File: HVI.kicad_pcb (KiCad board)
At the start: 2 copper layers, 48 x 48 mm, 47 parts, among them J1 Conn_01x02, J2 Conn_01x02, J3 Conn_01x02, U1 VIPER06-SSOP-10

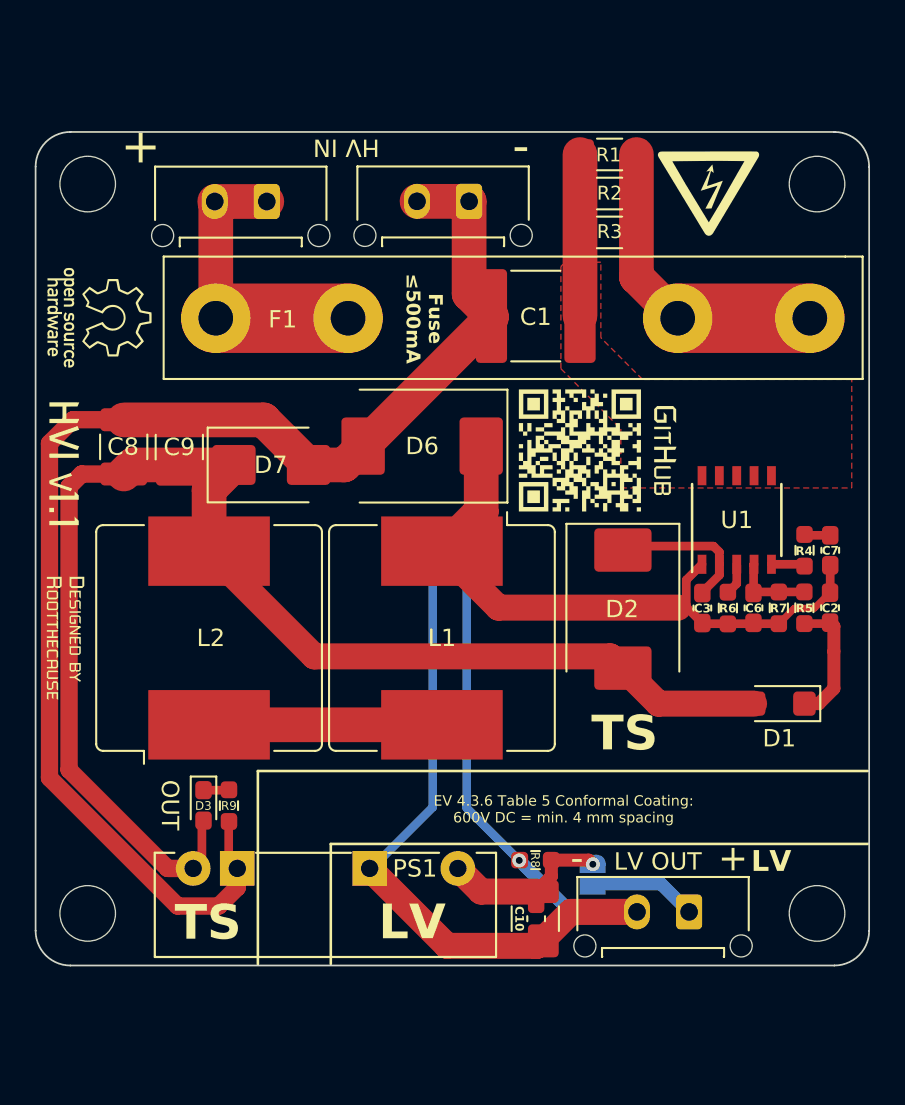
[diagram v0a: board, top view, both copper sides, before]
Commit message: Changed the connectors to Molex MicrofitPlus
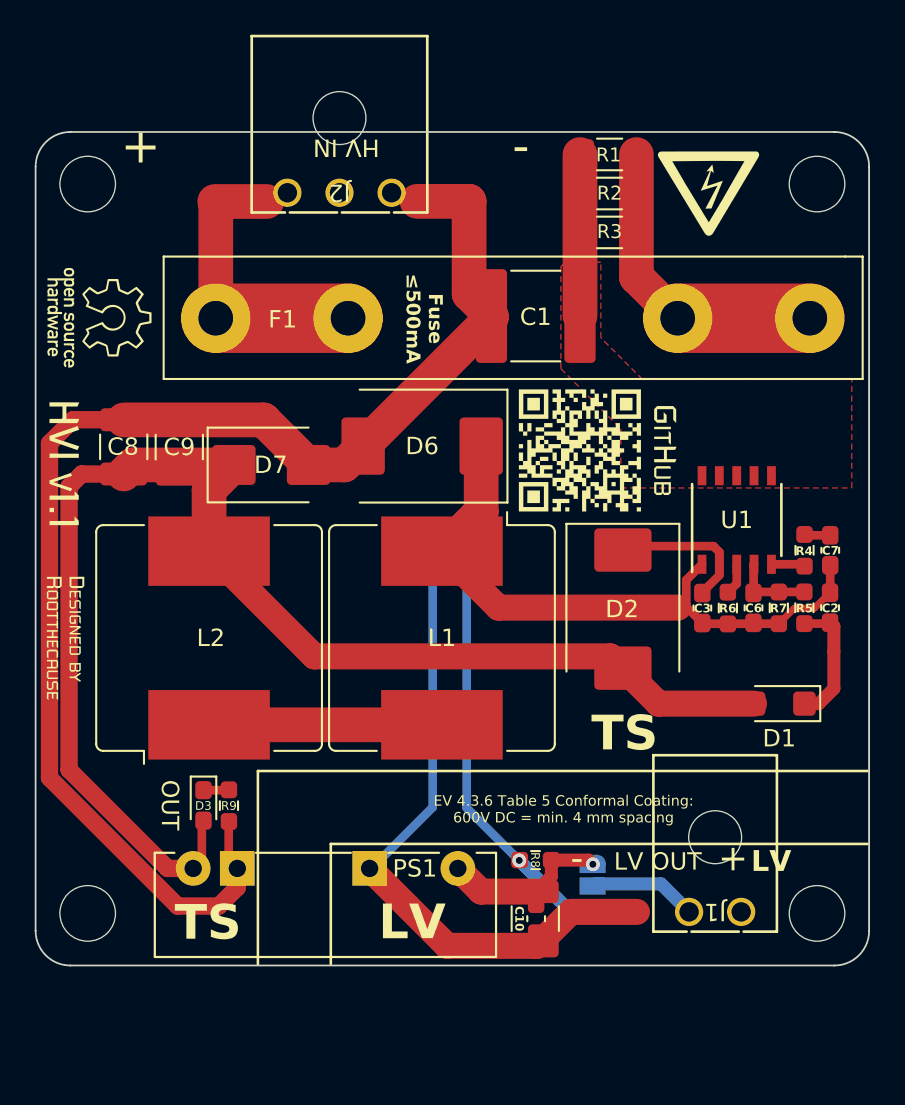
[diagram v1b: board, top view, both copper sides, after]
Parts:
- removed J3: Conn_01x02, Connector_Molex:Molex_Micro-Fit_3.0_43650-0215_1x02_P3.00mm_Vertical
- J1: footprint Connector_Molex:Molex_Micro-Fit_3.0_43650-0215_1x02_P3.00mm_Vertical -> yfs:MolexMicrofitPlus1x2
- J2: value Conn_01x02 -> Conn_01x03; footprint Connector_Molex:Molex_Micro-Fit_3.0_43650-0215_1x02_P3.00mm_Vertical -> yfs:MolexMicrofitPlus1x3
- PS1: value PEME1-S12-S5-S -> RP-1205S
- moved J2 1.29 mm to (84.5, 63.5)
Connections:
- F1 pad 1: Net-(J2-Pin_1) -> Net-(J2-Pin_3)
- J2 pad 1: Net-(J2-Pin_1) -> Net-(D6-A)
- J2 pad 2: Net-(J2-Pin_1) -> unconnected-(J2-Pin_2-Pad2)
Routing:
- net Net-(J2-Pin_3): track 0.00 -> 17.4 mm
- net Net-(J2-Pin_1): track 17.4 -> 0.00 mm

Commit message: Added the footprint of the new DC/DC converter and moved around the PCB a tad
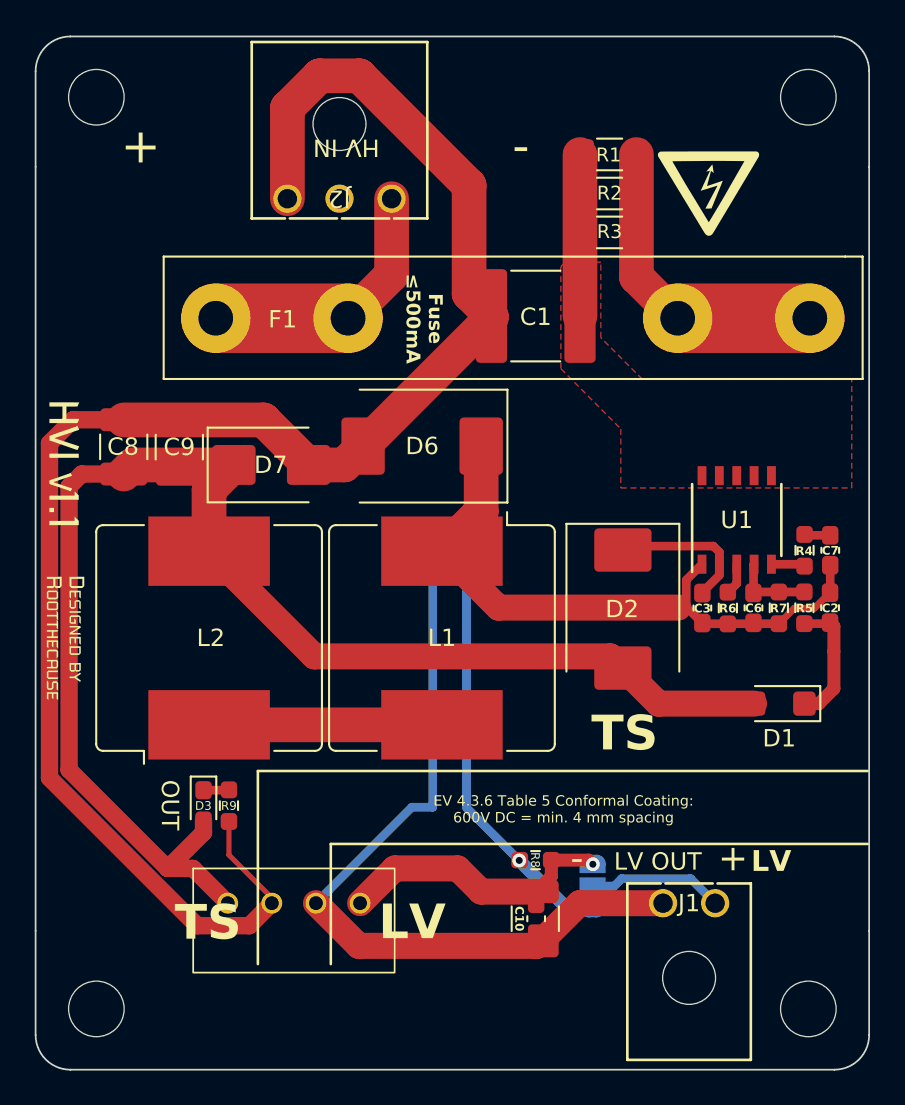
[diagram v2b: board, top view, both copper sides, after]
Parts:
- removed the G*** at (73.7, 70.7)
- removed the G*** at (106.3, 78.3)
- removed the G*** at (101.3, 78.3)
- PS1: value RP-1205S -> DRS1-12-S12-S; footprint Converter_DCDC:CONV_PEME1-S5-S5-S -> yfs:DCDC-12v_12v-DRS1-12-S12-S
- moved MK1 5.52 mm to (114.5, 110.5)
- moved MK4 5.52 mm to (73.5, 110.5)
- moved MK2 5.02 mm to (114.5, 58.0)
- moved MK3 5.02 mm to (73.5, 58.0)
- moved J1 1.58 mm to (109.1, 104.4), turned to 0 degrees
- moved J2 0.34 mm to (84.5, 63.8)
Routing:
- net Net-(D6-A): track 78.4 -> 99.6 mm
- net Net-(D5-K): track 37.1 -> 44.9 mm
- net Net-(JP1-A): track 9.72 -> 16.2 mm
- net Net-(D1-A): track 79.4 -> 83.0 mm
- net Net-(J2-Pin_3): track 17.4 -> 15.6 mm
- net Net-(J1-Pin_1): track 6.10 -> 7.82 mm
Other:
- board size 48 x 48 mm -> 48 x 59.5 mm

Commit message: Added silkscreen components, and ensured that it complied with the license
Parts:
- removed the G*** at (71.6, 89.6)
- removed the G*** at (71.7, 80.0)
- added G***: LOGO, LOGO, B.Cu at (111.0, 89.5)
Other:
- board text added: "Based on a design by Rootthecause"
- board text added: "Lenny Schwarz"
- board text added: "MAR 2026"
- board text added: "REV A"
- board text added: "TSAC LED"

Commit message: Changed the fuse
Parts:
- F1: footprint DC-DC Footprint Lib:Fuseholder0,25Zoll_32mm_littlefuse_102_122 -> Fuse:Fuseholder_Clip-5x20mm_Keystone_3512_Inline_P23.62x7.27mm_D1.02x1.57mm_Horizontal
- moved F1 5.82 mm to (74.7, 69.5)
- moved C1 5.81 mm to (104.0, 68.0), turned to -90 degrees
- moved G*** 4.48 mm to (112.5, 66.0)
- moved R1 3.79 mm to (103.1, 57.5)
- moved R2 3.79 mm to (103.0, 59.8)
- moved R3 3.78 mm to (103.0, 62.0)
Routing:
- net Net-(C1-Pad1): track 9.30 -> 25.1 mm
- net Net-(F1-Pad2): track 18.0 -> 29.1 mm, vias 0 -> 1
- net Net-(D6-A): track 99.6 -> 106.5 mm
- net Net-(J2-Pin_3): track 15.6 -> 18.2 mm
- removed copper zone on F.Cu, net Net-(C1-Pad1)
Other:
- board text added: "REV B"
- board text removed: "REV A"

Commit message: Ensured it based
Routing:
- net Net-(C1-Pad1): track 25.1 -> 29.1 mm
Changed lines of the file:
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@@
 			(unlocked yes)
 			(layer "F.SilkS")
+			(hide yes)
 			(effects
 				(font
@@
 			(unlocked yes)
 			(layer "F.Fab")
+			(hide yes)
 			(effects
 				(font
@@
 		(width 1)
 		(layer "F.Cu")
+		(net "Net-(C1-Pad1)")
+	)
+	(segment
+		(start 108.375 79.795)
+		(end 112.375 79.795)
+		(width 1)
+		(layer "F.Cu")

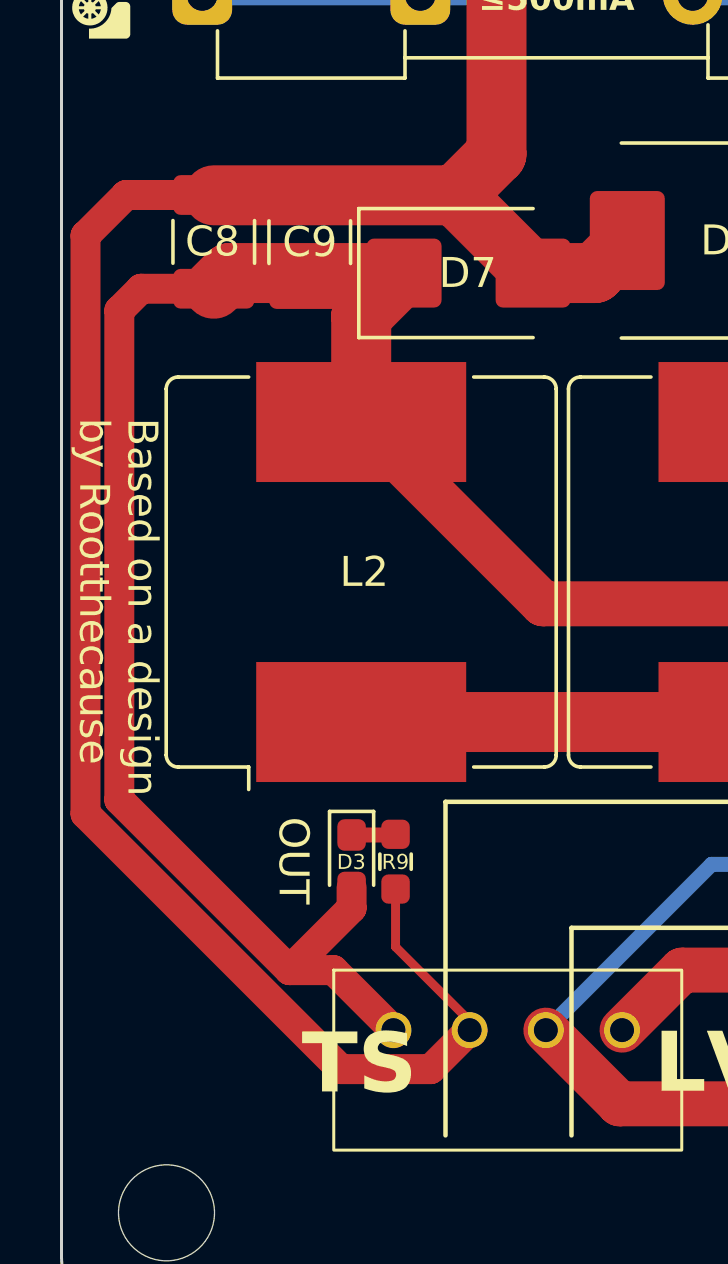
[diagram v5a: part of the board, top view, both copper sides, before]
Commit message: Changed the size of a couple of traces
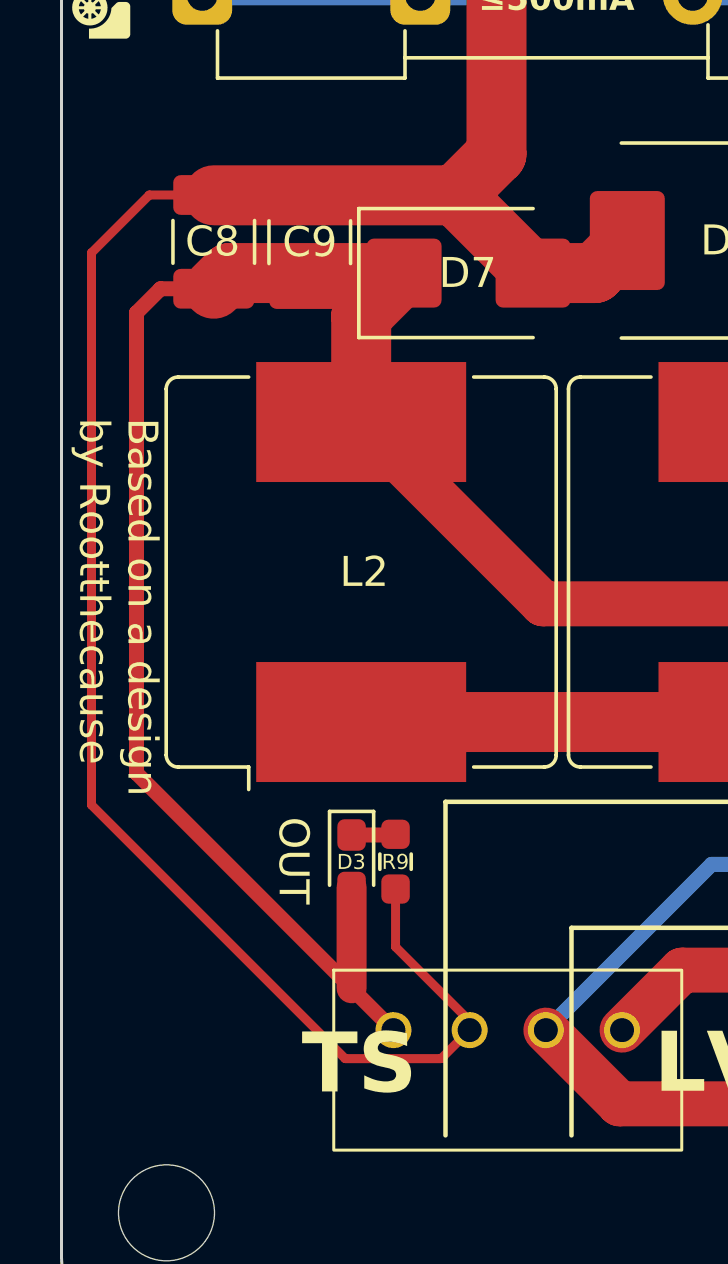
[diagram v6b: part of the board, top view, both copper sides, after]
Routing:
- net Net-(D1-A): track 83.0 -> 81.0 mm
- net Net-(D6-A): track 106.5 -> 105.3 mm
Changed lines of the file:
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@@
+	)
+	(segment
+		(start 79.67 99.655)
+		(end 79.67 103.015)
+		(width 1)
+		(layer "F.Cu")
+		(net "Net-(D1-A)")
 	)
 	(segment
@@
 	)
 	(segment
-		(start 72.6525 79.6975)
-		(end 75.075 79.6975)
-		(width 1)
-		(layer "F.Cu")
-		(net "Net-(D1-A)")
-	)
-	(segment
-		(start 79.67 100.343818)
-		(end 79.67 99.655)
-		(width 1)
-		(layer "F.Cu")
-		(net "Net-(D1-A)")
-	)
-	(segment
 		(start 103.1 90.2)
 		(end 103.9 91)
@@
 	)
 	(segment
-		(start 77.603818 102.41)
-		(end 79.67 100.343818)
-		(width 1)
-		(layer "F.Cu")
-		(net "Net-(D1-A)")
-	)
-	(segment
-		(start 79.065 102.41)
-		(end 81.065 104.41)
-		(width 1)
-		(layer "F.Cu")
-		(net "Net-(D1-A)")
-	)
-	(segment
 		(start 75.5975 79.175)
 		(end 75.075 79.6975)
@@
 	)
 	(segment
-		(start 77.603818 102.41)
-		(end 71.927 96.733182)
-		(width 1)
-		(layer "F.Cu")
-		(net "Net-(D1-A)")
-	)
-	(segment
-		(start 71.927 80.423)
-		(end 72.6525 79.6975)
-		(width 1)
+		(start 81.065 104.41)
+		(end 72.5 95.845)
+		(width 0.5)
 		(layer "F.Cu")
 		(net "Net-(D1-A)")
@@
 	)
 	(segment
-		(start 71.927 96.733182)
-		(end 71.927 80.423)
-		(width 1)
-		(layer "F.Cu")
-		(net "Net-(D1-A)")
-	)
-	(segment
 		(start 111.374 92.92)
 		(end 105.865 92.92)
@@
 	)
 	(segment
-		(start 77.603818 102.41)
-		(end 79.065 102.41)
-		(width 1)
+		(start 72.5 95.845)
+		(end 72.5 80.5)
+		(width 0.5)
+		(layer "F.Cu")
+		(net "Net-(D1-A)")
+	)
+	(segment
+		(start 73.3025 79.6975)
+		(end 75.075 79.6975)
+		(width 0.5)
+		(layer "F.Cu")
+		(net "Net-(D1-A)")
+	)
+	(segment
+		(start 72.5 80.5)
+		(end 73.3025 79.6975)
+		(width 0.5)
 		(layer "F.Cu")
 		(net "Net-(D1-A)")
@@
 	)
 	(segment
+		(start 71 78.5)
+		(end 72.9275 76.5725)
+		(width 0.3)
+		(layer "F.Cu")
+		(net "Net-(D6-A)")
+	)
+	(segment
 		(start 81.135 101.635)
 		(end 81.135 99.7075)
@@
 	)
 	(segment
-		(start 75.075 76.5725)
-		(end 72.1525 76.5725)
-		(width 1)
-		(layer "F.Cu")
-		(net "Net-(D6-A)")
-	)
-	(segment
 		(start 94.965 63.07945)
 		(end 88.650684 56.765134)
@@
 	)
 	(segment
+		(start 71 96.905026)
+		(end 71 78.5)
+		(width 0.3)
+		(layer "F.Cu")
+		(net "Net-(D6-A)")
+	)
+	(segment
 		(start 96.471912 63.07945)
 		(end 103.942462 70.55)
@@
 	)
 	(segment
-		(start 72.1525 76.5725)
-		(end 70.8 77.925)
-		(width 1)
-		(layer "F.Cu")
-		(net "Net-(D6-A)")
-	)
-	(segment
 		(start 86.349314 56.765134)
 		(end 84.5 58.614448)
@@
 	)
 	(segment
-		(start 82.305 105.71)
-		(end 83.605 104.41)
-		(width 1)
-		(layer "F.Cu")
-		(net "Net-(D6-A)")
-	)
-	(segment
-		(start 79.31 105.71)
-		(end 82.305 105.71)
-		(width 1)
+		(start 83.605 104.41)
+		(end 82.655 105.36)
+		(width 0.3)
 		(layer "F.Cu")
 		(net "Net-(D6-A)")
@@
 	)
 	(segment
-		(start 70.8 77.925)
-		(end 70.8 97.2)
-		(width 1)
+		(start 79.454974 105.36)
+		(end 71 96.905026)
+		(width 0.3)
 		(layer "F.Cu")
 		(net "Net-(D6-A)")
@@
 	)
 	(segment
-		(start 70.8 97.2)
-		(end 79.31 105.71)
-		(width 1)
+		(start 82.655 105.36)
+		(end 79.454974 105.36)
+		(width 0.3)
 		(layer "F.Cu")
 		(net "Net-(D6-A)")
@@
 		(layer "F.Cu")
 		(net "Net-(D6-A)")
+	)
+	(segment
+		(start 72.9275 76.5725)
+		(end 75.075 76.5725)
+		(width 0.3)
+		(layer "F.Cu")
+		(net "Net-(D6-A)")
